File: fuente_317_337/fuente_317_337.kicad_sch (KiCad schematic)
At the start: 51 parts, among them J1 Fuente, J11 GND, J14 +1.2V, J15 -1.2V, J2 Salida, J3 Salida_5v, J4 Salida_12v, J5 Cooler, J6 Inputs, SW1 SW_SPDT, U1 LM317_TO-220, U11 LM79L05, U4 LM7805_TO220, U5 LM385, U7 LM337_TO220

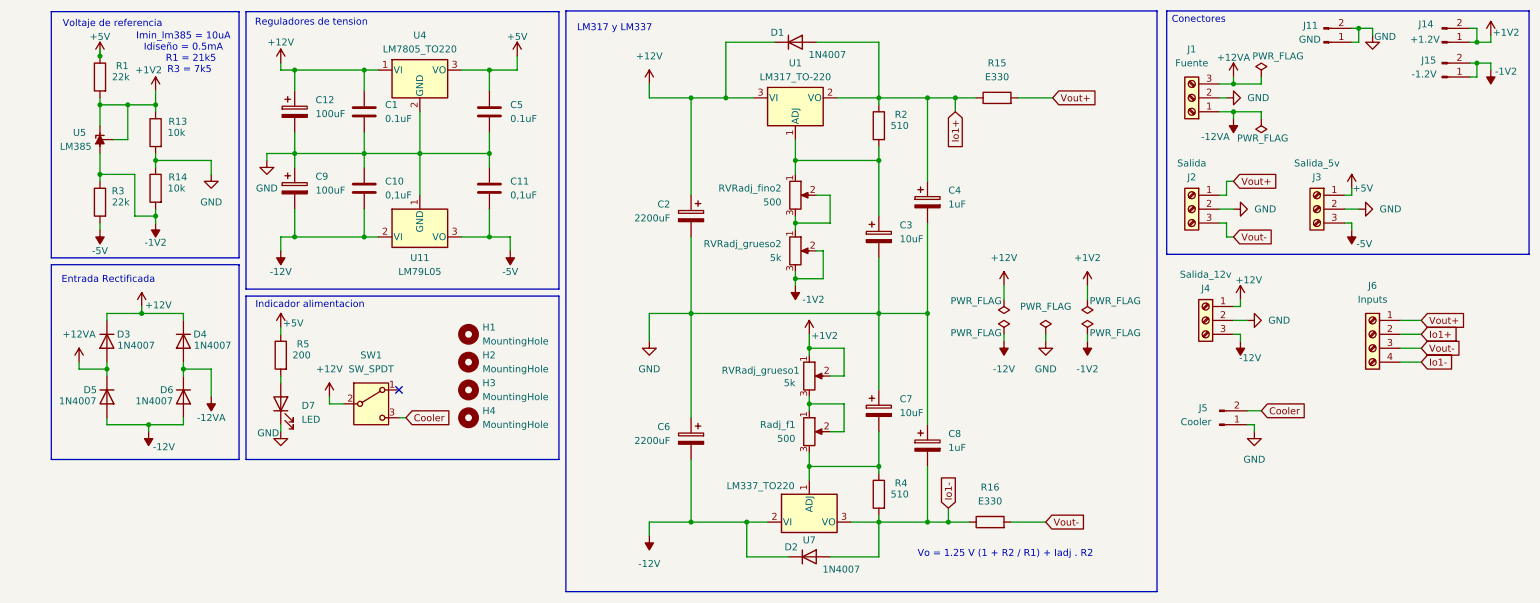
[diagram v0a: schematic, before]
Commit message: fuente_317_337: pcb finalizado de fuente y controlador
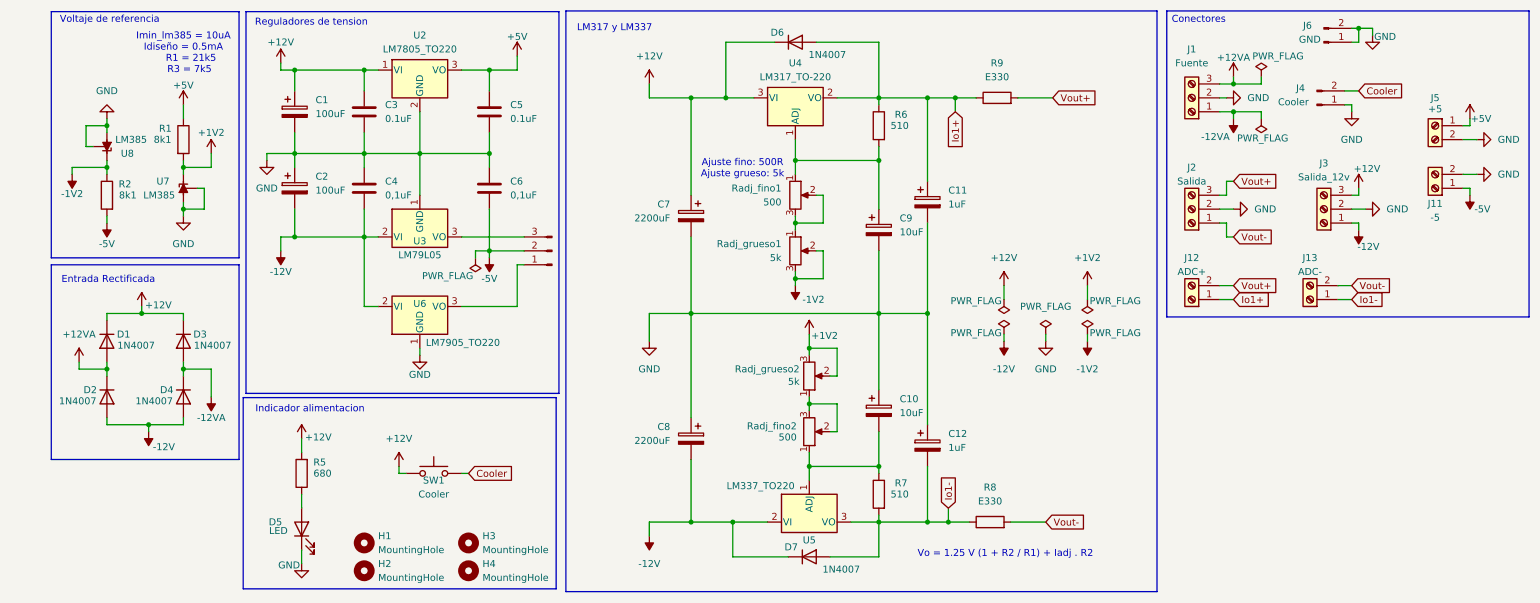
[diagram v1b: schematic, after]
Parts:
- removed C1: 0.1uF, Capacitor_THT:C_Disc_D3.0mm_W2.0mm_P2.50mm, symbol Device:C
- removed C10, C11: 0,1uF, Capacitor_THT:C_Disc_D3.0mm_W2.0mm_P2.50mm, symbol Device:C
- removed C3: 10uF, Capacitor_THT:CP_Radial_D5.0mm_P2.50mm, symbol Device:C_Polarized
- removed C4: 1uF, Capacitor_THT:CP_Radial_D5.0mm_P2.50mm, symbol Device:C_Polarized
- removed C6: 2200uF, Capacitor_THT:CP_Radial_D16.0mm_P7.50mm, symbol Device:C_Polarized
- removed D5: 1N4007, Diode_THT:D_DO-41_SOD81_P10.16mm_Horizontal, symbol Diode:1N4007
- removed D7: LED, LED_THT:LED_D5.0mm, symbol Device:LED
- removed J11: GND, Connector_PinHeader_2.54mm:PinHeader_1x02_P2.54mm_Vertical, symbol Connector:Conn_01x02_Pin
- removed J14: +1.2V, Connector_PinHeader_2.54mm:PinHeader_1x02_P2.54mm_Vertical, symbol Connector:Conn_01x02_Pin
- removed J15: -1.2V, Connector_PinHeader_2.54mm:PinHeader_1x02_P2.54mm_Vertical, symbol Connector:Conn_01x02_Pin
- removed J4: Salida_12v, TerminalBlock_Phoenix:TerminalBlock_Phoenix_MKDS-1,5-3-5.08_1x03_P5.08mm_Horizontal, symbol Connector:Screw_Terminal_01x03
- removed J5: Cooler, Connector_PinHeader_2.54mm:PinHeader_1x02_P2.54mm_Vertical, symbol Connector:Conn_01x02_Pin
- removed J6: Inputs, TerminalBlock_Phoenix:TerminalBlock_Phoenix_MKDS-1,5-4-5.08_1x04_P5.08mm_Horizontal, symbol Connector:Screw_Terminal_01x04
- removed R13, R14: 10k, Resistor_THT:R_Axial_DIN0207_L6.3mm_D2.5mm_P10.16mm_Horizontal, symbol Device:R
- removed R15, R16: E330, Resistor_THT:R_Axial_Power_L25.0mm_W6.4mm_P30.48mm, symbol Device:R
- removed R3: 22k, Resistor_THT:R_Axial_DIN0207_L6.3mm_D2.5mm_P10.16mm_Horizontal, symbol Device:R
- removed R4: 510, Resistor_THT:R_Axial_DIN0207_L6.3mm_D2.5mm_P10.16mm_Horizontal, symbol Device:R
- removed RVRadj_fino2, Radj_f1: 500, Connector_PinHeader_2.54mm:PinHeader_1x03_P2.54mm_Vertical, symbol Device:R_Potentiometer
- removed RVRadj_grueso1, RVRadj_grueso2: 5k, Connector_PinHeader_2.54mm:PinHeader_1x03_P2.54mm_Vertical, symbol Device:R_Potentiometer
- removed SW1: SW_SPDT, Connector_PinHeader_2.54mm:PinHeader_1x03_P2.54mm_Vertical, symbol Switch:SW_SPDT
- removed U1: LM317_TO-220, Package_TO_SOT_THT:TO-220-3_Vertical, symbol Regulator_Linear:LM317_TO-220
- removed U11: LM79L05, Package_TO_SOT_THT:TO-92_Inline, symbol Regulator_Linear:L7905
- removed U4: LM7805_TO220, Package_TO_SOT_THT:TO-220-3_Vertical, symbol Regulator_Linear:LM7805_TO220
- removed U5: LM385, Package_TO_SOT_THT:TO-92_Inline, symbol Reference_Voltage:TL431LP
- removed U7: LM337_TO220, Package_TO_SOT_THT:TO-220-3_Vertical, symbol Regulator_Linear:LM337_TO220
- added C1: 100uF, Capacitor_THT:CP_Radial_D5.0mm_P2.50mm, symbol Device:C_Polarized
- added C10: 10uF, Capacitor_THT:CP_Radial_D5.0mm_P2.50mm, symbol Device:C_Polarized
- added C11: 1uF, Capacitor_THT:CP_Radial_D5.0mm_P2.50mm, symbol Device:C_Polarized
- added C3: 0.1uF, Capacitor_THT:C_Disc_D3.0mm_W2.0mm_P2.50mm, symbol Device:C
- added C4, C6: 0,1uF, Capacitor_THT:C_Disc_D3.0mm_W2.0mm_P2.50mm, symbol Device:C
- added D5: LED, LED_THT:LED_D5.0mm, symbol Device:LED
- added D7: 1N4007, Diode_THT:D_DO-41_SOD81_P10.16mm_Horizontal, symbol Diode:1N4007
- added J10: SEL_7905, Connector_PinHeader_2.54mm:PinHeader_1x03_P2.54mm_Vertical, symbol Connector:Conn_01x03_Pin
- added J11: -5, TerminalBlock_Phoenix:TerminalBlock_Phoenix_MKDS-1,5-2-5.08_1x02_P5.08mm_Horizontal, symbol Connector:Screw_Terminal_01x02
- added J12: ADC+, TerminalBlock_Phoenix:TerminalBlock_Phoenix_MKDS-1,5-2-5.08_1x02_P5.08mm_Horizontal, symbol Connector:Screw_Terminal_01x02
- added J13: ADC-, TerminalBlock_Phoenix:TerminalBlock_Phoenix_MKDS-1,5-2-5.08_1x02_P5.08mm_Horizontal, symbol Connector:Screw_Terminal_01x02
- added J4: Cooler, Connector_PinHeader_2.54mm:PinHeader_1x02_P2.54mm_Vertical, symbol Connector:Conn_01x02_Pin
- added J5: +5, TerminalBlock_Phoenix:TerminalBlock_Phoenix_MKDS-1,5-2-5.08_1x02_P5.08mm_Horizontal, symbol Connector:Screw_Terminal_01x02
- added J6: GND, Connector_PinHeader_2.54mm:PinHeader_1x02_P2.54mm_Vertical, symbol Connector:Conn_01x02_Pin
- added R6: 510, Resistor_THT:R_Axial_DIN0207_L6.3mm_D2.5mm_P2.54mm_Vertical, symbol Device:R
- added R7: 510, Resistor_THT:R_Axial_DIN0207_L6.3mm_D2.5mm_P10.16mm_Horizontal, symbol Device:R
- added R8, R9: E330, Resistor_THT:R_Axial_Power_L25.0mm_W6.4mm_P30.48mm, symbol Device:R
- added Radj_fino1, Radj_fino2: 500, Connector_PinHeader_2.54mm:PinHeader_1x03_P2.54mm_Vertical, symbol Device:R_Potentiometer
- added Radj_grueso1, Radj_grueso2: 5k, Connector_PinHeader_2.54mm:PinHeader_1x03_P2.54mm_Vertical, symbol Device:R_Potentiometer
- added SW1: Cooler, Connector_PinHeader_2.54mm:PinHeader_1x02_P2.54mm_Vertical, symbol Switch:SW_Push
- added U2: LM7805_TO220, Package_TO_SOT_THT:TO-220-3_Vertical, symbol Regulator_Linear:LM7805_TO220
- added U3: LM79L05, Package_TO_SOT_THT:TO-92_Inline, symbol Regulator_Linear:L7905
- added U4: LM317_TO-220, Package_TO_SOT_THT:TO-220-3_Vertical, symbol Regulator_Linear:LM317_TO-220
- added U5: LM337_TO220, Package_TO_SOT_THT:TO-220-3_Vertical, symbol Regulator_Linear:LM337_TO220
- added U6: LM7905_TO220, Package_TO_SOT_THT:TO-220-3_Vertical, symbol Regulator_Linear:LM7905_TO220
- added U7, U8: LM385, Package_TO_SOT_THT:TO-92_Inline, symbol Reference_Voltage:TL431LP
- C12: value 100uF -> 1uF
- C2: value 2200uF -> 100uF; footprint Capacitor_THT:CP_Radial_D16.0mm_P7.50mm -> Capacitor_THT:CP_Radial_D5.0mm_P2.50mm
- C7: value 10uF -> 2200uF; footprint Capacitor_THT:CP_Radial_D5.0mm_P2.50mm -> Capacitor_THT:CP_Radial_D16.0mm_P7.50mm
- C8: value 1uF -> 2200uF; footprint Capacitor_THT:CP_Radial_D5.0mm_P2.50mm -> Capacitor_THT:CP_Radial_D16.0mm_P7.50mm
- C9: value 100uF -> 10uF
- J3: value Salida_5v -> Salida_12v
- R1: value 22k -> 8k1
- R2: value 510 -> 8k1; footprint Resistor_THT:R_Axial_DIN0207_L6.3mm_D2.5mm_P10.16mm_Horizontal -> Resistor_THT:R_Axial_DIN0207_L6.3mm_D2.5mm_P5.08mm_Vertical
- R5: value 200 -> 680
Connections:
- net +12V: now also C7.1, D6.1 (K), J3.3 (Pin_3), R5.2, C1.1, C3.1, SW1.1, U2.1 (VI), U4.3 (VI); no longer C12.1, C2.1, D4.1 (K)
- net +12VA: now also D1.2 (A), D2.1 (K); no longer D3.2 (A)
- net +1V2: now also Radj_grueso2.2, Radj_grueso2.3, U7.3 (K)
- net +5V: now also J5.1 (Pin_1), U2.3 (VO); no longer J3.1 (Pin_1), R5.1
- net -12V: now also C2.2, C8.2, D2.2 (A), D4.2 (A), J3.1 (Pin_1), C4.2, D7.1 (K), U3.2 (VI), U5.2 (VI), U6.2 (VI); no longer C9.2, D2.1 (K), D6.2 (A)
- net -12VA: now also D3.2 (A), D4.1 (K); no longer D4.2 (A), D6.1 (K)
- net -1V2: now also R2.1, Radj_grueso1.2, Radj_grueso1.3, U8.3 (K)
- net -5V: now also R2.2, C6.2, J10.2 (Pin_2), J11.1 (Pin_1); no longer J3.3 (Pin_3)
- net Cooler: now also J4.2 (Pin_2), SW1.2
- net GND: now also C12.1, C2.1, C7.2, C9.2, C1.2, C10.1, C11.2, C3.2, C4.1, C6.1, D5.1 (K), J11.2 (Pin_2), J4.1 (Pin_1), J5.2 (Pin_2), J6.1 (Pin_1), J6.2 (Pin_2), U2.2 (GND), U3.1 (GND), U6.1 (GND), U7.1 (REF), U7.2 (A), U8.1 (REF), U8.2 (A); no longer C12.2, C2.2, C7.1, C9.1
- net Io1+: now also D6.2 (A), C11.1, J12.1 (Pin_1), R6.1, R9.1, U4.2 (VO); no longer D1.2 (A), R2.1
- net Io1-: now also C12.2, D7.2 (A), J13.1 (Pin_1), R7.2, R8.1, U5.3 (VO); no longer C8.2, D2.2 (A)
- net Vout+: now also J2.3 (Pin_3), J12.2 (Pin_2), R9.2; no longer J2.1 (Pin_1)
- net Vout-: now also J2.1 (Pin_1), J13.2 (Pin_2), R8.2; no longer J2.3 (Pin_3)
- new net: C9.1, R6.2, Radj_fino1.1, U4.1 (ADJ)
- new net: Radj_fino1.2, Radj_fino1.3, Radj_grueso1.1
- new net: C10.2, R7.1, Radj_fino2.1, U5.1 (ADJ)
- new net: Radj_fino2.2, Radj_fino2.3, Radj_grueso2.1
- new net: D5.2 (A), R5.1
- new net: J10.3 (Pin_3), U3.3 (VO)
- new net: J10.1 (Pin_1), U6.3 (VO)
- no-connect marks 1 -> 0
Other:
- note added: "Ajuste fino: 500R Ajuste grueso: 5k"

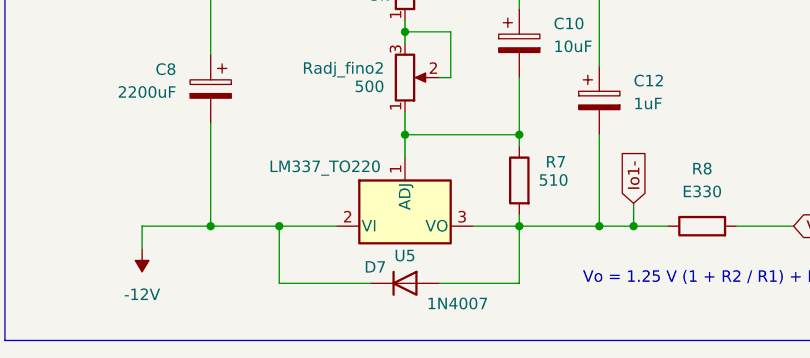
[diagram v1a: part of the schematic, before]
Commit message: fix: protection diode
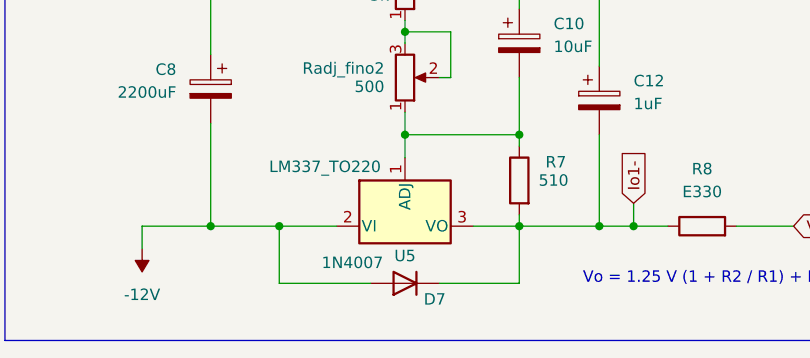
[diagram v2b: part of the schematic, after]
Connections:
- net -12V: now also D7.2 (A); no longer D7.1 (K)
- net Io1-: now also D7.1 (K); no longer D7.2 (A)
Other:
- moved on the sheet: D7
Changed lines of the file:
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@@
 		)
 		(instances
-			(project ""
+			(project "fuente_317_337"
 				(path "/1529c77d-439e-4034-a8ae-e3c6a5487580"
 					(reference "Radj_fino1")
@@
 		)
 		(instances
-			(project ""
+			(project "fuente_317_337"
 				(path "/1529c77d-439e-4034-a8ae-e3c6a5487580"
 					(reference "J5")
@@
 	(symbol
 		(lib_id "Diode:1N4007")
-		(at 152.4 113.03 0)
+		(at 152.4 113.03 180)
 		(unit 1)
 		(exclude_from_sim no)
@@
 		(dnp no)
 		(property "Reference" "D7"
-			(at 149.098 111.252 0)
+			(at 155.702 114.808 0)
 			(effects
 				(font
@@
 		)
 		(property "Value" "1N4007"
-			(at 158.242 115.316 0)
+			(at 146.558 110.744 0)
 			(effects
 				(font
@@
 		)
 		(property "Footprint" "Diode_THT:D_DO-41_SOD81_P10.16mm_Horizontal"
-			(at 152.4 117.475 0)
+			(at 152.4 108.585 0)
 			(effects
 				(font
@@
 		)
 		(instances
-			(project ""
+			(project "fuente_317_337"
 				(path "/1529c77d-439e-4034-a8ae-e3c6a5487580"
 					(reference "J10")
@@
 		)
 		(instances
-			(project ""
+			(project "fuente_317_337"
 				(path "/1529c77d-439e-4034-a8ae-e3c6a5487580"
 					(reference "SW1")
@@
 		)
 		(instances
-			(project ""
+			(project "fuente_317_337"
 				(path "/1529c77d-439e-4034-a8ae-e3c6a5487580"
 					(reference "U6")

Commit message: feat: version final para el tp integrador
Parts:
- removed U7, U8: LM385, Package_TO_SOT_THT:TO-92_Inline, symbol Reference_Voltage:TL431LP
- added U1, U7: LM385BZ-1.2, Package_TO_SOT_THT:TO-92_Inline, symbol Reference_Voltage:LM385BZ-1.2
- R1, R2: value 8k1 -> 10k
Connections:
- net +1V2: now also U7.2 (K)
- net -1V2: now also U1.3 (A)
- net GND: now also U1.2 (K), U7.3 (A)
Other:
- moved on the sheet: R1
